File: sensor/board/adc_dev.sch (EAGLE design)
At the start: 42 parts, among them Q2 MC-306 32.7680K-A0, U1 FT232RL-BASICSSOP

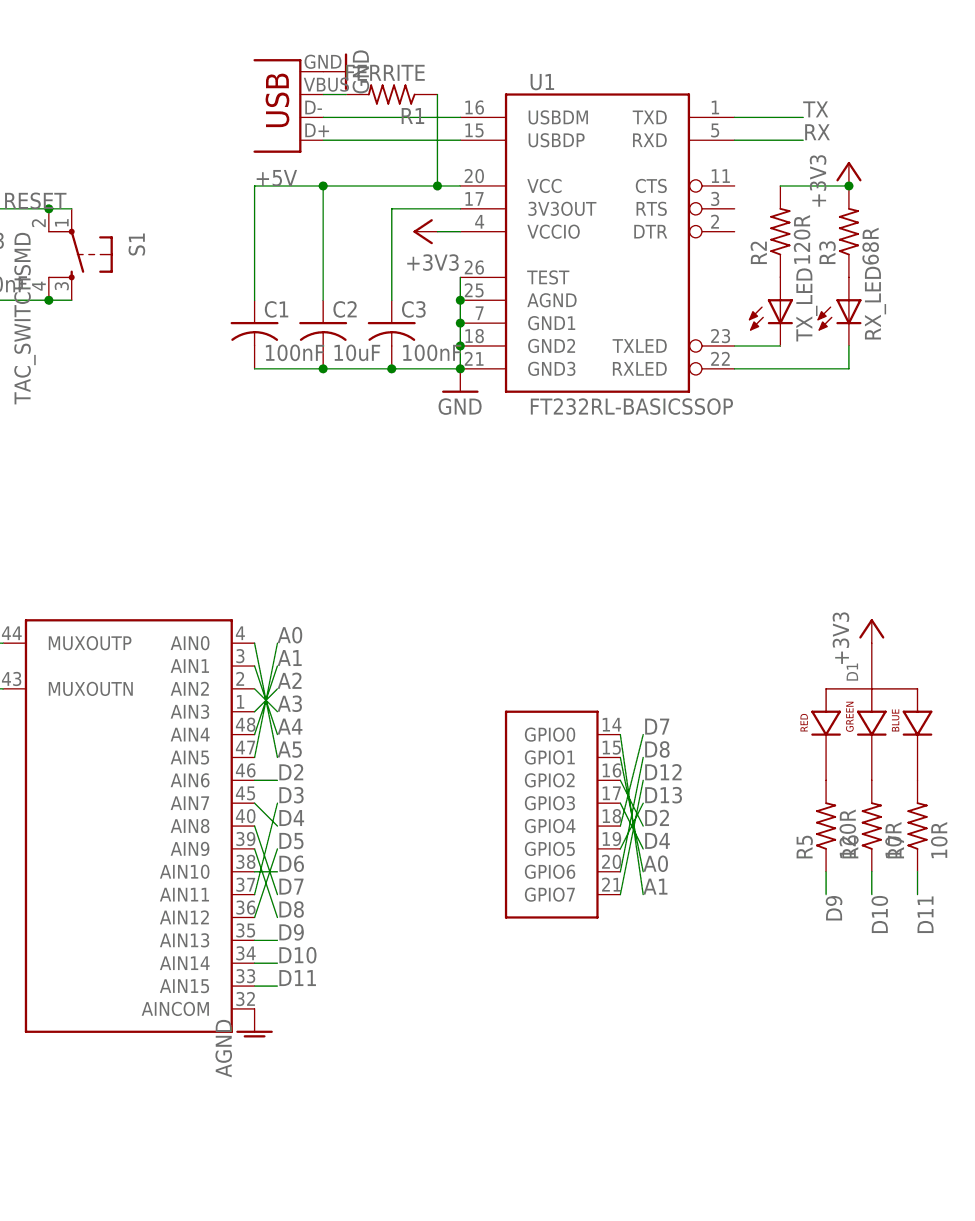
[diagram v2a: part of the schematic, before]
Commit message: Layout pretty much done, need to clean up schematic and do silkscreen
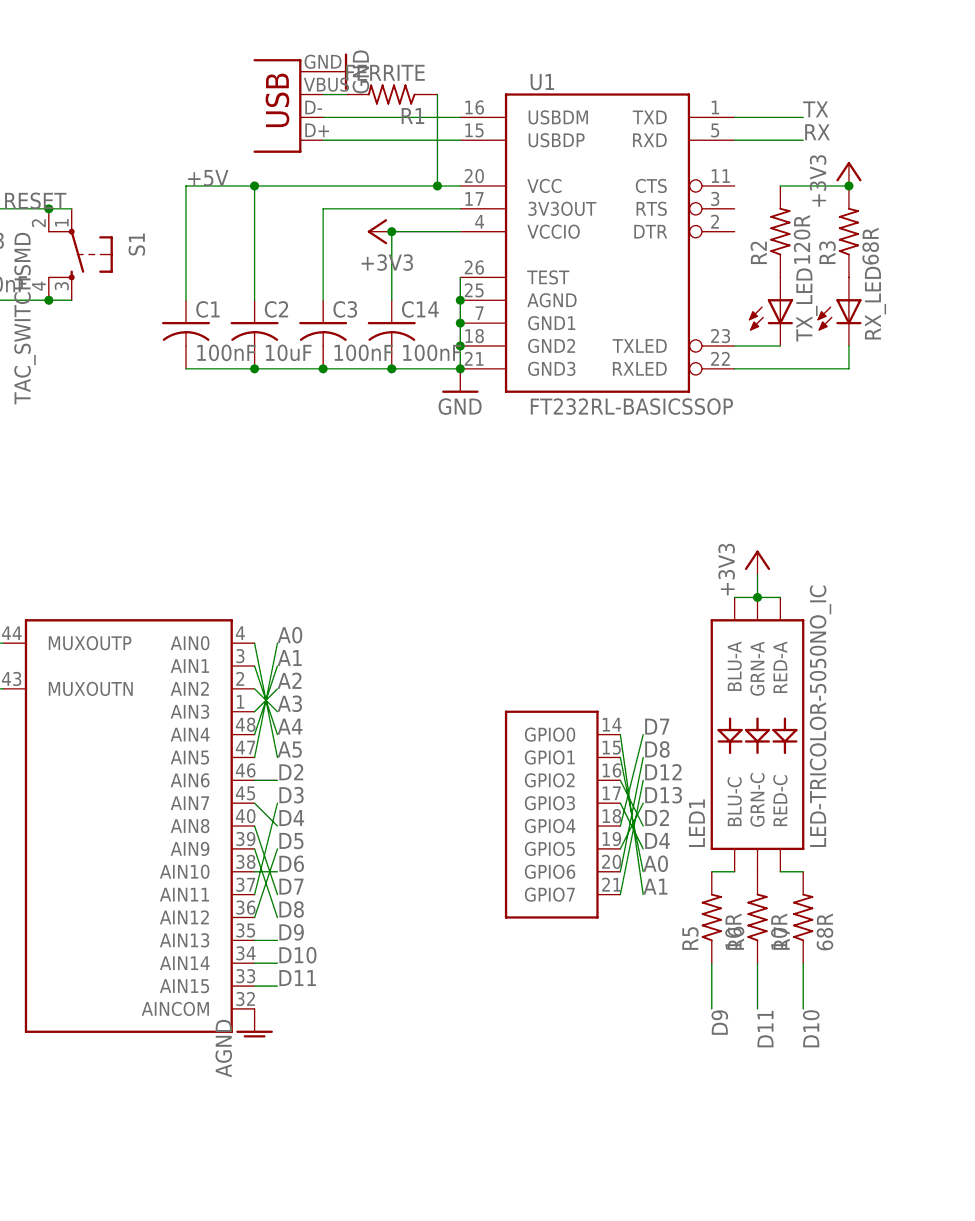
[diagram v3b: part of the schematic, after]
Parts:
- removed D1: LED-RGB-CA-THRUCLEAR, SparkFun-LED:LED-RGB-CA-THRUCLEAR
- added C14: 100nF, rcl:C-USC0603
- added LED1: LED-TRICOLOR-5050NO_IC, SparkFun-LED:LED-TRICOLOR-5050NO_IC
- JP3: value USB-B -> USBSMD; device SparkFun-Connectors:USBPTH -> SparkFun-Connectors:USBSMD
- R5: value 120R -> 10R
- R7: value 10R -> 68R
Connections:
- net +3V3: now also C14.1, LED1.BLU-A, LED1.GRN-A, LED1.RED-A; no longer D1.ANODE
- net D10: now also R7.1; no longer R6.1
- net D11: now also R6.1; no longer R7.1
- net GND: now also C14.2
- net N$17: now also LED1.BLU-C; no longer D1.RED_CATHODE
- net N$18: now also LED1.GRN-C; no longer D1.GREEN_CATHODE
- net N$21: now also LED1.RED-C; no longer D1.BLUE_CATHODE
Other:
- moved on the sheet: C1, C2, C3, R5, R6, R7
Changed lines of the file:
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@@
 <part name="U$1" library="modular_robotics" deviceset="ADS1258" device=""/>
 <part name="U$2" library="SparkFun-Boards" deviceset="ARDUINO_R3_SHIELD" device=""/>
-<part name="JP3" library="SparkFun-Connectors" deviceset="USB" device="PTH" value="USB-B"/>
+<part name="JP3" library="SparkFun-Connectors" deviceset="USB" device="SMD" value="USBSMD"/>
 <part name="U1" library="SparkFun-DigitalIC" deviceset="FT232RL-BASIC" device="SSOP"/>
 <part name="R1" library="rcl" deviceset="R-US_" device="R0603" value="FERRITE"/>
@@
 <part name="JP5" library="pinhead" deviceset="PINHD-1X2" device=""/>
 <part name="Q2" library="crystal" deviceset="MC-306" device="" value="MC-306 32.7680K-A0"/>
-<part name="D1" library="SparkFun-LED" deviceset="LED-RGB-CA-THRU" device="CLEAR"/>
 <part name="+3V12" library="supply1" deviceset="+3V3" device=""/>
-<part name="R5" library="rcl" deviceset="R-US_" device="R0603" value="120R"/>
+<part name="R5" library="rcl" deviceset="R-US_" device="R0603" value="10R"/>
 <part name="R6" library="rcl" deviceset="R-US_" device="R0603" value="10R"/>
-<part name="R7" library="rcl" deviceset="R-US_" device="R0603" value="10R"/>
+<part name="R7" library="rcl" deviceset="R-US_" device="R0603" value="68R"/>
 <part name="R8" library="rcl" deviceset="R-US_" device="R0603" value="4k7"/>
 <part name="R9" library="rcl" deviceset="R-US_" device="R0603" value="4k7"/>
 <part name="+3V13" library="supply1" deviceset="+3V3" device=""/>
+<part name="LED1" library="SparkFun-LED" deviceset="LED-TRICOLOR-5050" device="NO_IC"/>
+<part name="C14" library="rcl" deviceset="C-US" device="C0603" value="100nF"/>
 </parts>
 <sheets>
@@
 <instance part="TX_LED" gate="G$1" x="226.06" y="147.32"/>
 <instance part="RX_LED" gate="G$1" x="233.68" y="147.32"/>
-<instance part="+3V1" gate="G$1" x="185.42" y="154.94" rot="R90"/>
+<instance part="+3V1" gate="G$1" x="180.34" y="154.94" rot="R90"/>
 <instance part="GND1" gate="1" x="190.5" y="137.16"/>
-<instance part="C1" gate="G$1" x="167.64" y="144.78"/>
-<instance part="C2" gate="G$1" x="175.26" y="144.78"/>
-<instance part="C3" gate="G$1" x="182.88" y="144.78"/>
+<instance part="C1" gate="G$1" x="160.02" y="144.78"/>
+<instance part="C2" gate="G$1" x="167.64" y="144.78"/>
+<instance part="C3" gate="G$1" x="175.26" y="144.78"/>
 <instance part="GND2" gate="1" x="177.8" y="172.72" rot="R90"/>
 <instance part="+3V2" gate="G$1" x="233.68" y="162.56"/>
@@
 <instance part="JP5" gate="G$1" x="63.5" y="139.7"/>
 <instance part="Q2" gate="P" x="50.8" y="101.6" rot="R90"/>
-<instance part="D1" gate="G$1" x="236.22" y="99.06" rot="R90"/>
-<instance part="+3V12" gate="G$1" x="236.22" y="111.76"/>
-<instance part="R5" gate="G$1" x="231.14" y="88.9" rot="R90"/>
-<instance part="R6" gate="G$1" x="236.22" y="88.9" rot="R90"/>
-<instance part="R7" gate="G$1" x="241.3" y="88.9" rot="R90"/>
+<instance part="+3V12" gate="G$1" x="223.52" y="119.38"/>
+<instance part="R5" gate="G$1" x="218.44" y="78.74" rot="R90"/>
+<instance part="R6" gate="G$1" x="223.52" y="78.74" rot="R90"/>
+<instance part="R7" gate="G$1" x="228.6" y="78.74" rot="R90"/>
 <instance part="U$1" gate="EPAD" x="81.28" y="139.7" rot="R180"/>
 <instance part="R8" gate="G$1" x="129.54" y="15.24" rot="R90"/>
 <instance part="R9" gate="G$1" x="137.16" y="15.24" rot="R90"/>
 <instance part="+3V13" gate="G$1" x="137.16" y="22.86"/>
+<instance part="LED1" gate="D1" x="223.52" y="99.06" rot="R90"/>
+<instance part="C14" gate="G$1" x="182.88" y="144.78"/>
 </instances>
 <busses>
@@
 <pinref part="C2" gate="G$1" pin="2"/>
 <wire x1="182.88" y1="139.7" x2="175.26" y2="139.7" width="0.1524" layer="91"/>
-<junction x="182.88" y="139.7"/>
-<pinref part="C1" gate="G$1" pin="2"/>
 <wire x1="175.26" y1="139.7" x2="167.64" y2="139.7" width="0.1524" layer="91"/>
 <junction x="175.26" y="139.7"/>
+<pinref part="C1" gate="G$1" pin="2"/>
+<wire x1="167.64" y1="139.7" x2="160.02" y2="139.7" width="0.1524" layer="91"/>
+<junction x="167.64" y="139.7"/>
+<pinref part="C14" gate="G$1" pin="2"/>
+<junction x="182.88" y="139.7"/>
 </segment>
 <segment>
@@
 <pinref part="U1" gate="G$1" pin="VCCIO"/>
 <pinref part="+3V1" gate="G$1" pin="+3V3"/>
-<wire x1="187.96" y1="154.94" x2="190.5" y2="154.94" width="0.1524" layer="91"/>
+<wire x1="182.88" y1="154.94" x2="190.5" y2="154.94" width="0.1524" layer="91"/>
+<pinref part="C14" gate="G$1" pin="1"/>
+<wire x1="182.88" y1="147.32" x2="182.88" y2="154.94" width="0.1524" layer="91"/>
+<junction x="182.88" y="154.94"/>
 </segment>
 <segment>
@@
 </segment>
 <segment>
-<pinref part="D1" gate="G$1" pin="ANODE"/>
-<pinref part="+3V12" gate="G$1" pin="+3V3"/>
-</segment>
-<segment>
 <pinref part="R9" gate="G$1" pin="2"/>
 <pinref part="+3V13" gate="G$1" pin="+3V3"/>
@@
 <junction x="137.16" y="20.32"/>
 </segment>
+<segment>
+<pinref part="LED1" gate="D1" pin="GRN-A"/>
+<pinref part="+3V12" gate="G$1" pin="+3V3"/>
+<wire x1="223.52" y1="116.84" x2="223.52" y2="114.3" width="0.1524" layer="91"/>
+<pinref part="LED1" gate="D1" pin="BLU-A"/>
+<wire x1="220.98" y1="114.3" x2="223.52" y2="114.3" width="0.1524" layer="91"/>
+<junction x="223.52" y="114.3"/>
+<pinref part="LED1" gate="D1" pin="RED-A"/>
+<wire x1="223.52" y1="114.3" x2="226.06" y2="114.3" width="0.1524" layer="91"/>
+</segment>
 </net>
 <net name="N$5" class="0">
@@
 <pinref part="U1" gate="G$1" pin="3V3OUT"/>
 <pinref part="C3" gate="G$1" pin="1"/>
-<wire x1="190.5" y1="157.48" x2="182.88" y2="157.48" width="0.1524" layer="91"/>
-<wire x1="182.88" y1="157.48" x2="182.88" y2="147.32" width="0.1524" layer="91"/>
+<wire x1="190.5" y1="157.48" x2="175.26" y2="157.48" width="0.1524" layer="91"/>
+<wire x1="175.26" y1="157.48" x2="175.26" y2="147.32" width="0.1524" layer="91"/>
 </segment>
 </net>
@@
 <pinref part="C1" gate="G$1" pin="1"/>
 <wire x1="190.5" y1="160.02" x2="187.96" y2="160.02" width="0.1524" layer="91"/>
-<wire x1="187.96" y1="160.02" x2="175.26" y2="160.02" width="0.1524" layer="91"/>
-<wire x1="175.26" y1="160.02" x2="167.64" y2="160.02" width="0.1524" layer="91"/>
-<wire x1="167.64" y1="160.02" x2="167.64" y2="147.32" width="0.1524" layer="91"/>
+<wire x1="187.96" y1="160.02" x2="167.64" y2="160.02" width="0.1524" layer="91"/>
+<wire x1="167.64" y1="160.02" x2="160.02" y2="160.02" width="0.1524" layer="91"/>
+<wire x1="160.02" y1="160.02" x2="160.02" y2="147.32" width="0.1524" layer="91"/>
 <pinref part="C2" gate="G$1" pin="1"/>
-<wire x1="175.26" y1="147.32" x2="175.26" y2="160.02" width="0.1524" layer="91"/>
-<junction x="175.26" y="160.02"/>
+<wire x1="167.64" y1="147.32" x2="167.64" y2="160.02" width="0.1524" layer="91"/>
+<junction x="167.64" y="160.02"/>
 <pinref part="R1" gate="G$1" pin="1"/>
 <wire x1="187.96" y1="170.18" x2="187.96" y2="160.02" width="0.1524" layer="91"/>
 <junction x="187.96" y="160.02"/>
-<label x="167.64" y="160.02" size="1.778" layer="95"/>
+<label x="160.02" y="160.02" size="1.778" layer="95"/>
 </segment>
 <segment>
@@
 <segment>
 <pinref part="R5" gate="G$1" pin="1"/>
-<wire x1="231.14" y1="83.82" x2="231.14" y2="81.28" width="0.1524" layer="91"/>
-<label x="231.14" y="81.28" size="1.778" layer="95" rot="R270"/>
+<wire x1="218.44" y1="73.66" x2="218.44" y2="68.58" width="0.1524" layer="91"/>
+<label x="218.44" y="68.58" size="1.778" layer="95" rot="R270"/>
 </segment>
 </net>
@@
 </segment>
 <segment>
-<pinref part="R6" gate="G$1" pin="1"/>
-<wire x1="236.22" y1="83.82" x2="236.22" y2="81.28" width="0.1524" layer="91"/>
-<label x="236.22" y="81.28" size="1.778" layer="95" rot="R270"/>
+<pinref part="R7" gate="G$1" pin="1"/>
+<wire x1="228.6" y1="73.66" x2="228.6" y2="68.58" width="0.1524" layer="91"/>
+<label x="228.6" y="68.58" size="1.778" layer="95" rot="R270"/>
 </segment>
 </net>
@@
 </segment>
 <segment>
-<pinref part="R7" gate="G$1" pin="1"/>
-<wire x1="241.3" y1="83.82" x2="241.3" y2="81.28" width="0.1524" layer="91"/>
-<label x="241.3" y="81.28" size="1.778" layer="95" rot="R270"/>
+<pinref part="R6" gate="G$1" pin="1"/>
+<wire x1="223.52" y1="73.66" x2="223.52" y2="68.58" width="0.1524" layer="91"/>
+<label x="223.52" y="68.58" size="1.778" layer="95" rot="R270"/>
 </segment>
 </net>
@@
 <net name="N$17" class="0">
 <segment>
-<pinref part="D1" gate="G$1" pin="RED_CATHODE"/>
+<pinref part="LED1" gate="D1" pin="BLU-C"/>
 <pinref part="R5" gate="G$1" pin="2"/>
+<wire x1="218.44" y1="83.82" x2="220.98" y2="83.82" width="0.1524" layer="91"/>
 </segment>
 </net>
 <net name="N$18" class="0">
 <segment>
-<pinref part="D1" gate="G$1" pin="GREEN_CATHODE"/>
+<pinref part="LED1" gate="D1" pin="GRN-C"/>
 <pinref part="R6" gate="G$1" pin="2"/>
 </segment>
@@
 <net name="N$21" class="0">
 <segment>
-<pinref part="D1" gate="G$1" pin="BLUE_CATHODE"/>
+<pinref part="LED1" gate="D1" pin="RED-C"/>
 <pinref part="R7" gate="G$1" pin="2"/>
-</segment>
-</net>
+<wire x1="228.6" y1="83.82" x2="226.06" y2="83.82" width="0.1524" layer="91"/>
+</segment>
+</net>

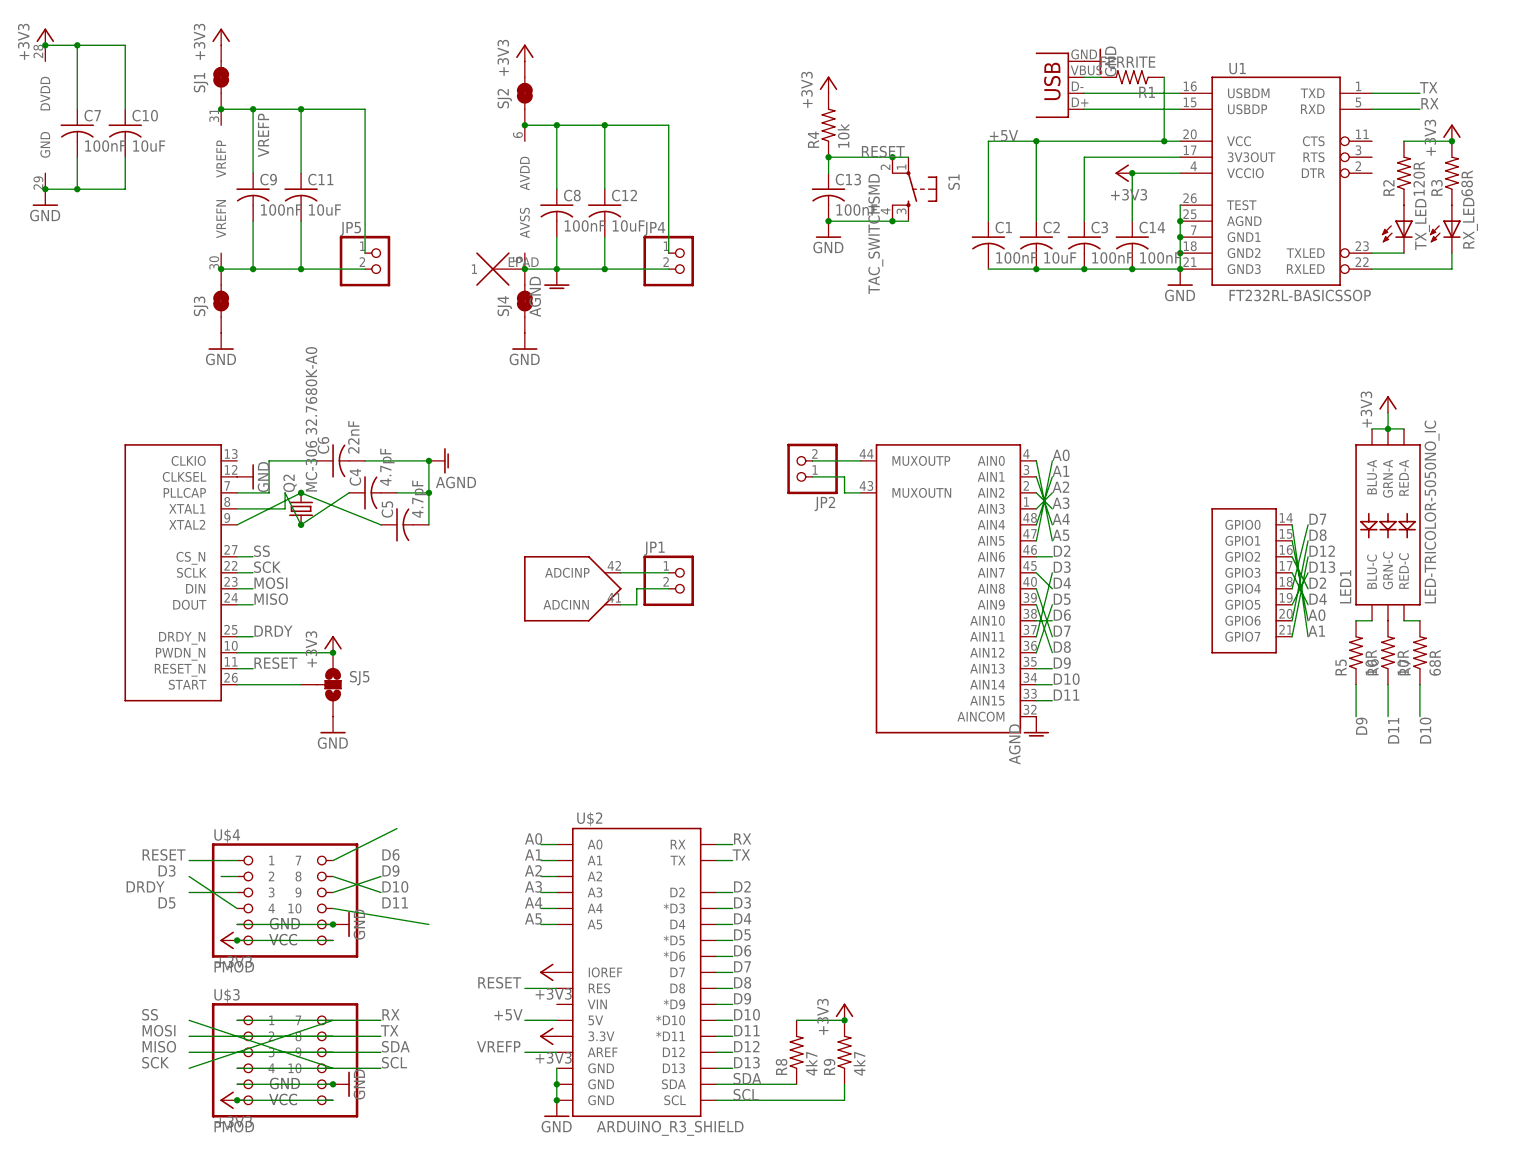
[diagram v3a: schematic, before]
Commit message: Tweak capacitor, made BLDC + ADC panel.
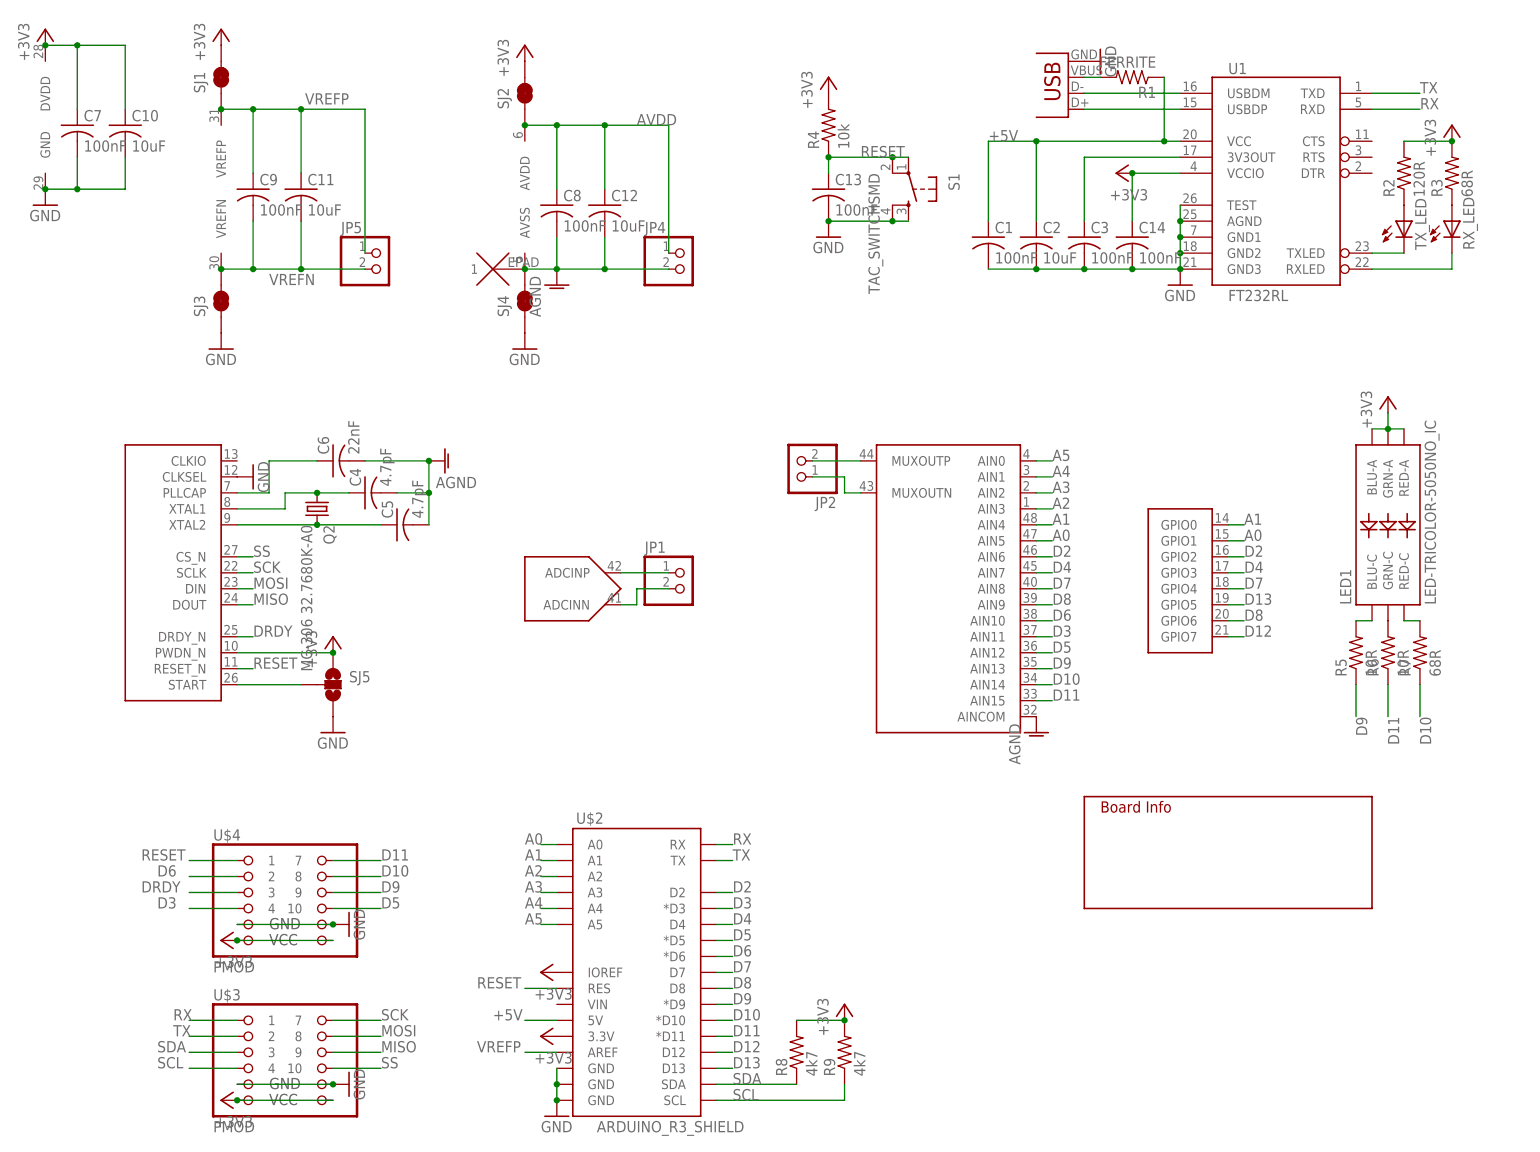
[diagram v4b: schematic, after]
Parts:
- added U$5: INFO, modular_robotics:INFO
- U1: value FT232RL-BASICSSOP -> FT232RL
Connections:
- net N$10 renamed ADCP
- net N$11 renamed AVDD
- net N$12 renamed VREFN
- net N$16 renamed ADCN
- net N$19 renamed MUXP
- net N$20 renamed MUXN
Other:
- moved on the sheet: Q2
